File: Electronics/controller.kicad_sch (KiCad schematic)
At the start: 22 parts, among them J101 Conn_01x06_Female, J102 Conn_01x06_Female, Q101 2N7002, Q102 2N7002, Q103 IRF9540NPBF, Q104 IRF9540NPBF

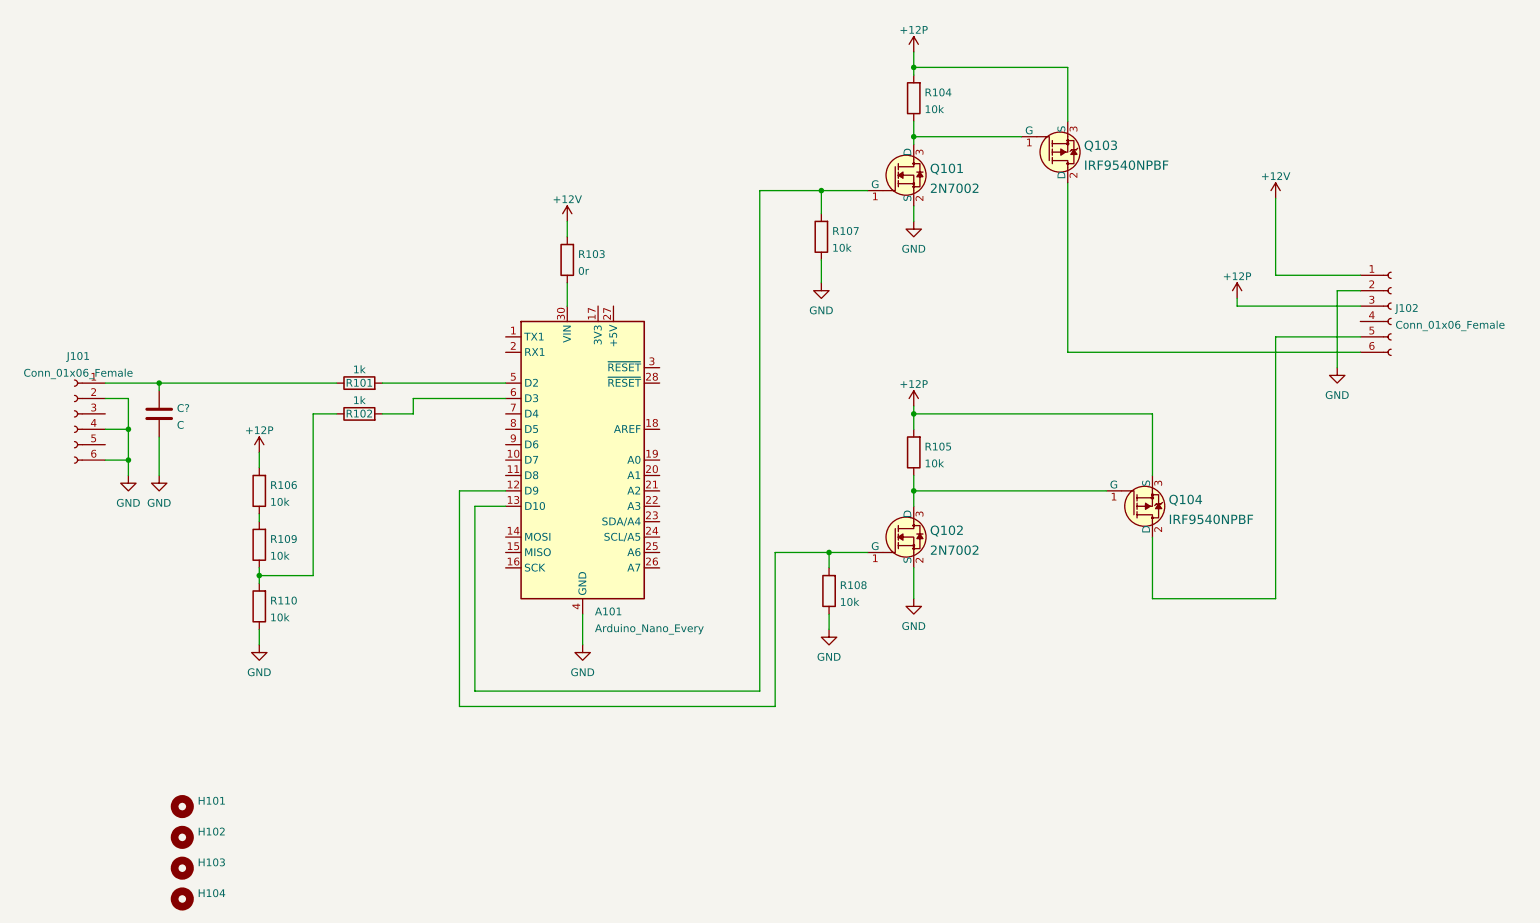
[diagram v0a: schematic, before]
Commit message: Hbridge addition
Signed-off-by: Finder <aki.kuusela@findersee.fi>
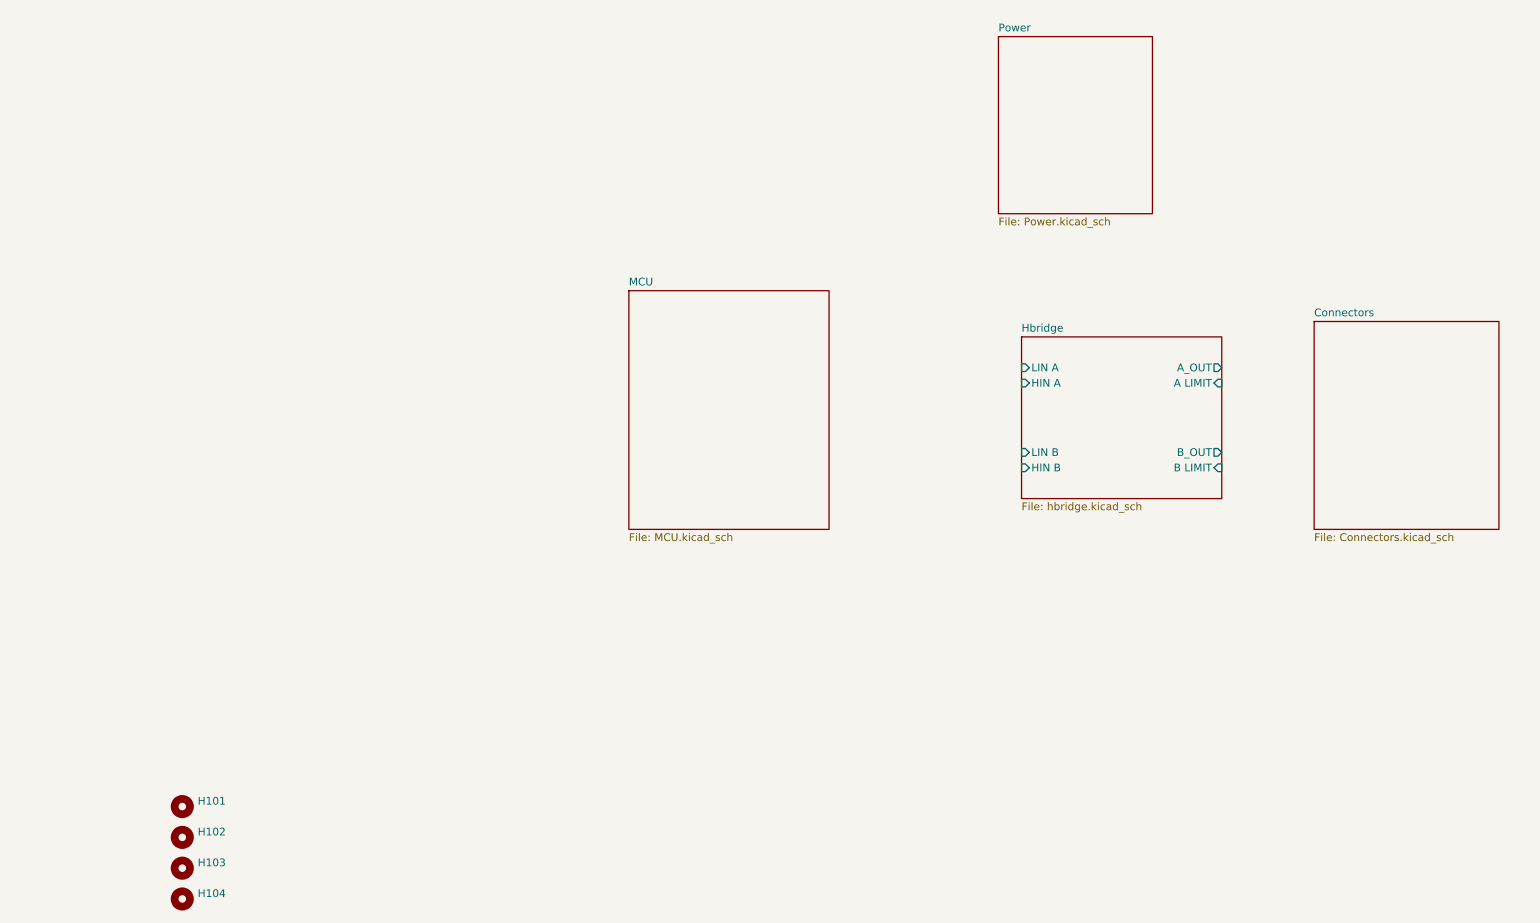
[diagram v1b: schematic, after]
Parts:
- removed A101: Arduino_Nano_Every, Module:Arduino_Nano, symbol MCU_Module:Arduino_Nano_Every
- removed C?: C, symbol Device:C
- removed J101, J102: Conn_01x06_Female, TerminalBlock:TerminalBlock_bornier-6_P5.08mm, symbol Connector:Conn_01x06_Female
- removed Q101, Q102: 2N7002, digikey-footprints:SOT-23-3, symbol dk_Transistors-FETs-MOSFETs-Single:2N7002
- removed Q103, Q104: IRF9540NPBF, digikey-footprints:TO-220-3, symbol dk_Transistors-FETs-MOSFETs-Single:IRF9540NPBF
- removed R101, R102: 1k, digikey-footprints:0603, symbol Device:R
- removed R103: 0r, digikey-footprints:0805, symbol Device:R
- removed R104, R105, R106, R107, R108, R109, R110: 10k, digikey-footprints:0603, symbol Device:R
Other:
- added sheet Connectors (Connectors.kicad_sch)
- added sheet Hbridge (hbridge.kicad_sch)
- added sheet MCU (MCU.kicad_sch)
- added sheet Power (Power.kicad_sch)

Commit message: Added third half bridge for BLDC applications
Signed-off-by: Finder <aki.kuusela@findersee.fi>
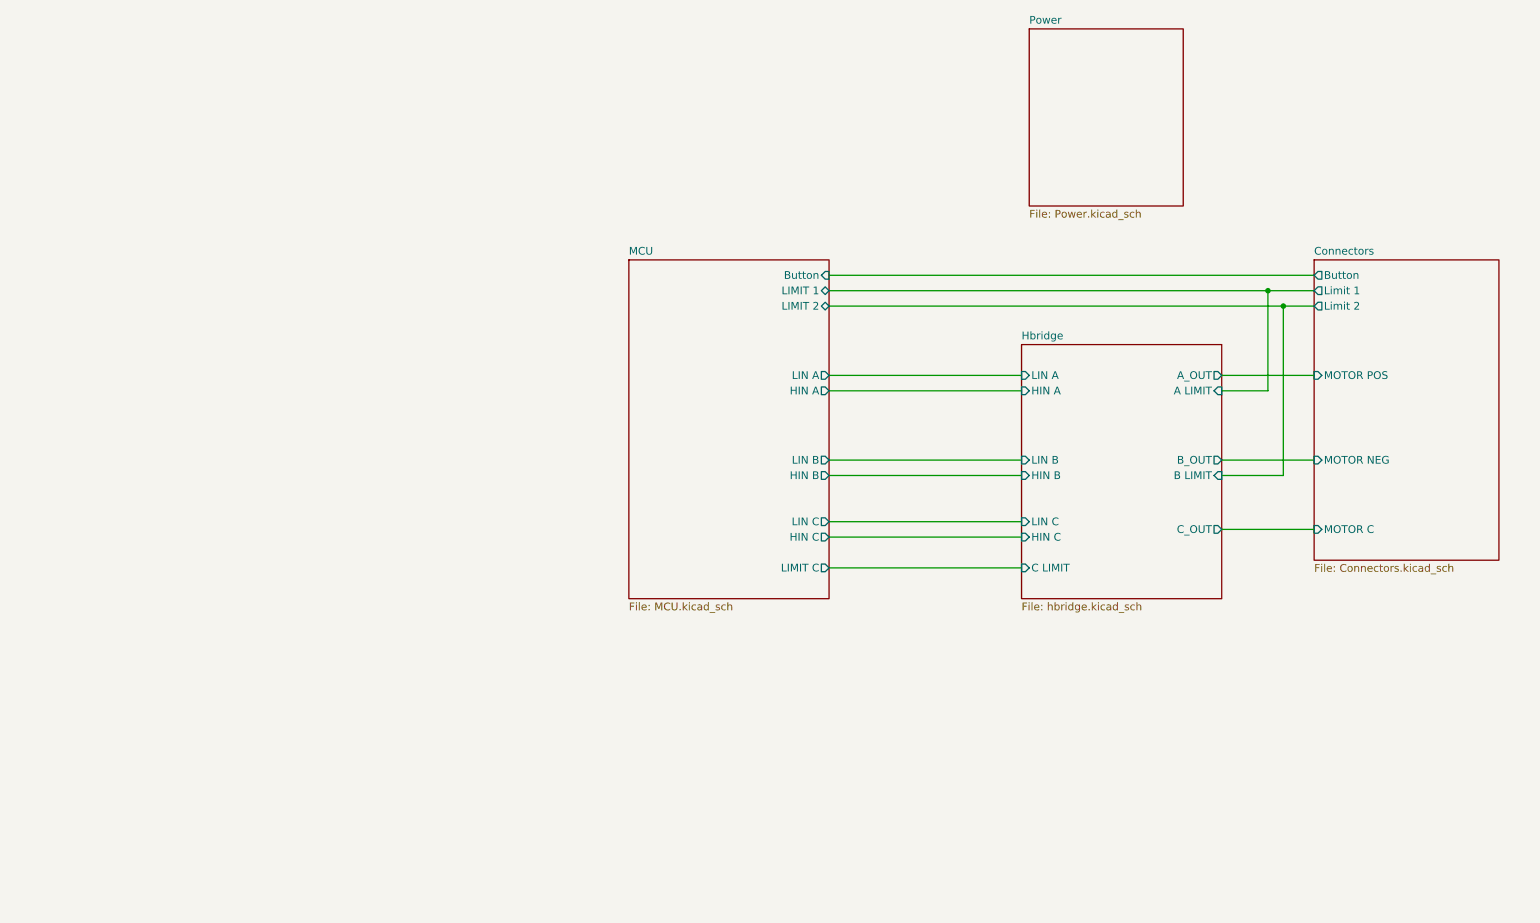
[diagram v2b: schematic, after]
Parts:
- removed H101, H102, H103, H104: MountingHole, MountingHole:MountingHole_3.2mm_M3, symbol Mechanical:MountingHole
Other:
- sheet Connectors ports: added Button, Limit 1, Limit 2, MOTOR C, MOTOR NEG, MOTOR POS; removed none
- sheet Hbridge ports: added C LIMIT, C_OUT, HIN C, LIN C; removed none
- sheet MCU ports: added Button, HIN A, HIN B, HIN C, LIMIT 1, LIMIT 2, LIMIT C, LIN A, LIN B, LIN C; removed none

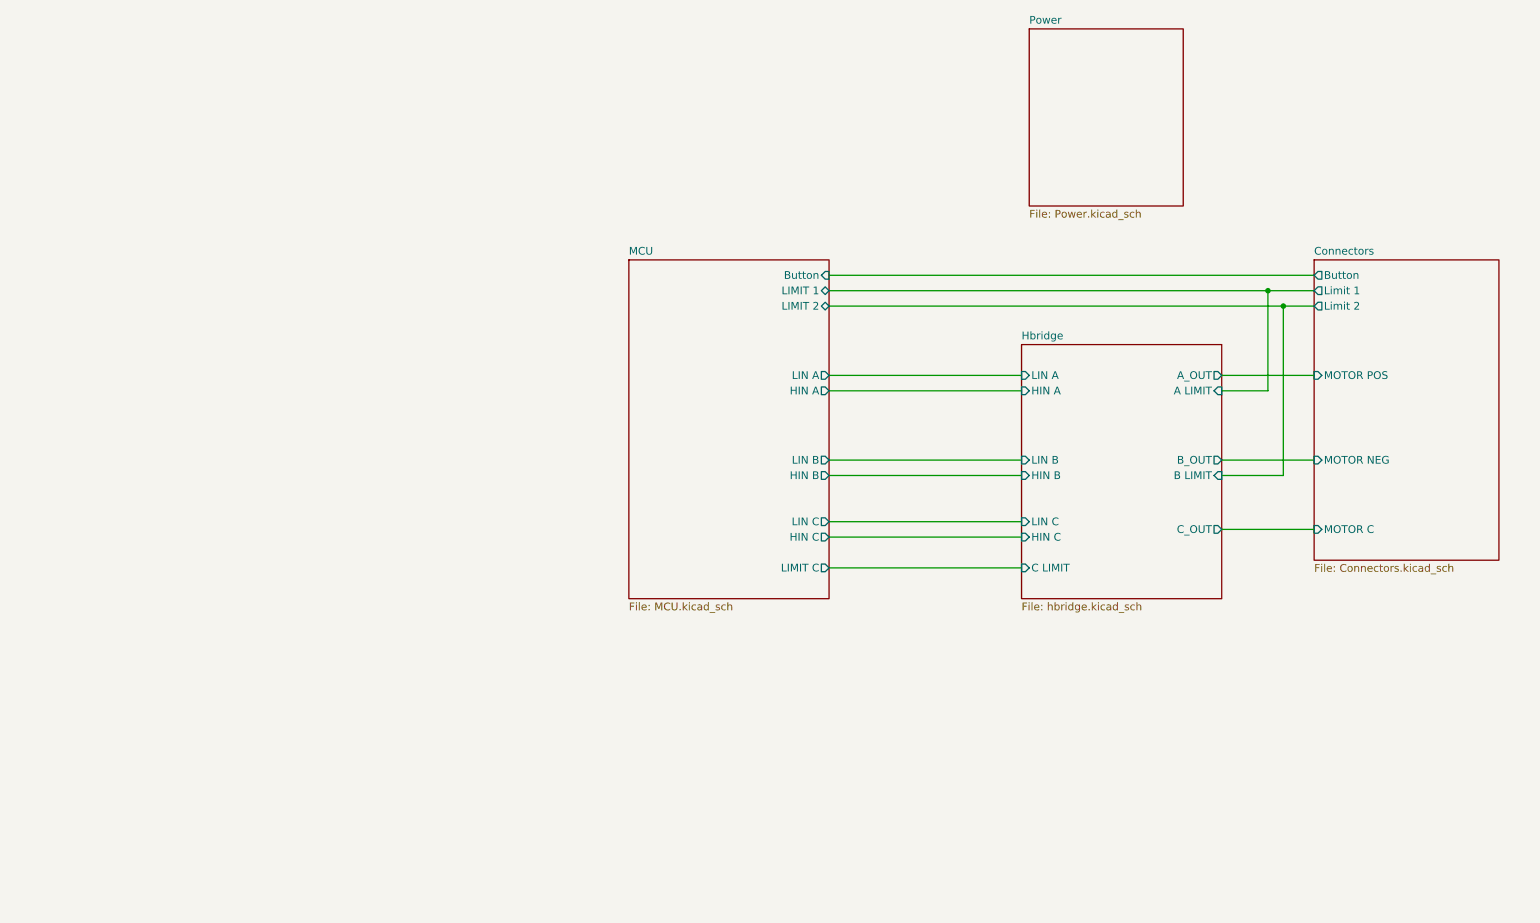
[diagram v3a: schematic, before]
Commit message: Added hall sensor circuitry
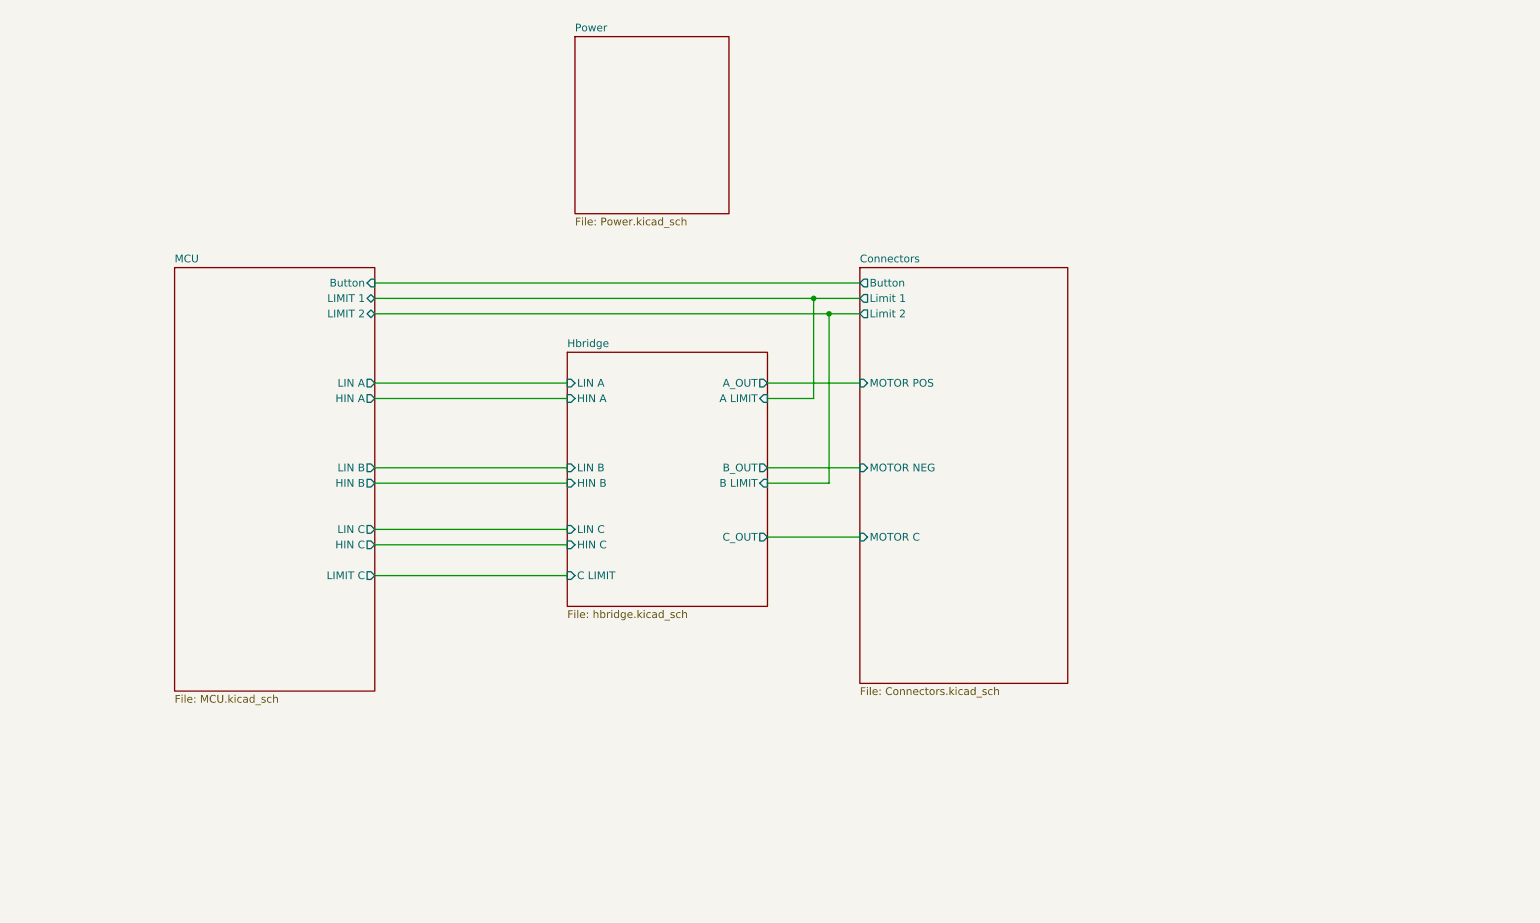
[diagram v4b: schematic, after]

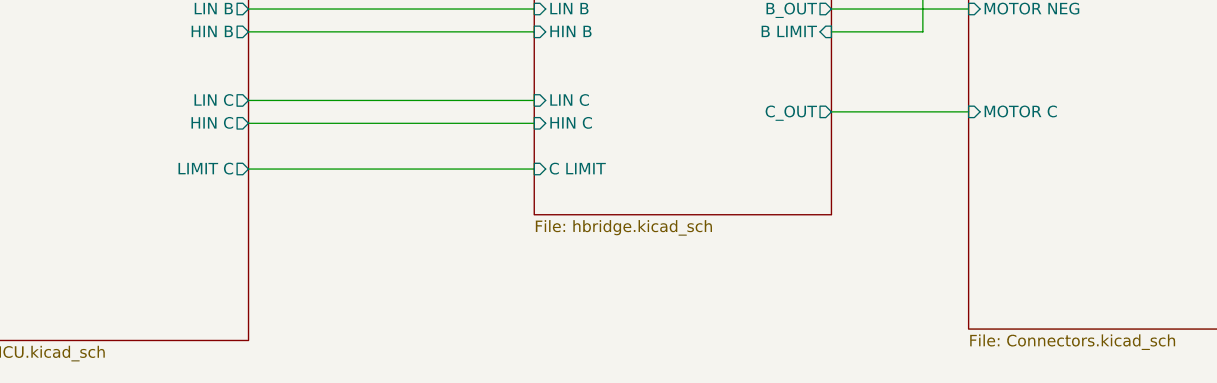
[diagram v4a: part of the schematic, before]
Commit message: Added Current sensor finalized layout version 0.1
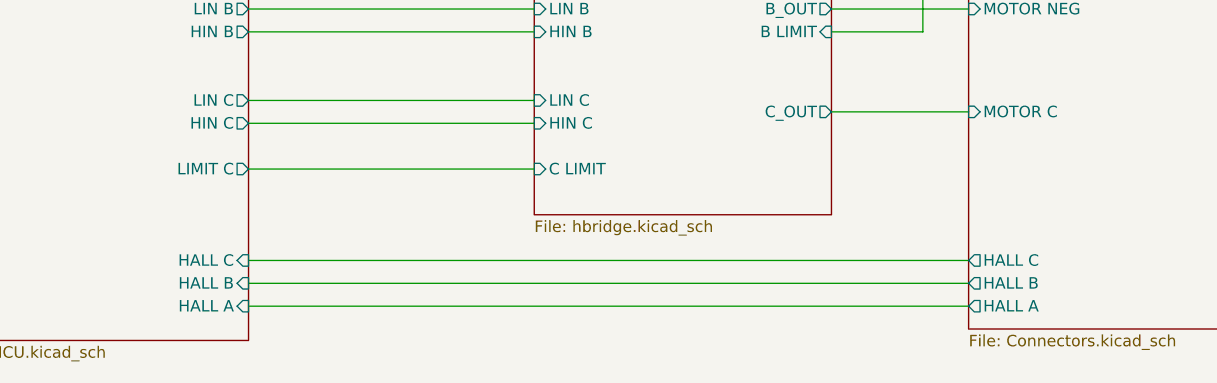
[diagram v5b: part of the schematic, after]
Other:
- sheet Connectors ports: added HALL A, HALL B, HALL C; removed none
- sheet MCU ports: added HALL A, HALL B, HALL C; removed none

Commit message: Updated Design
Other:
- sheet Connectors ports: added Latch Reset, VIOUT; removed none
- sheet MCU ports: added Latch Reset, V IOUT; removed none
